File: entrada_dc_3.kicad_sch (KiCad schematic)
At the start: 4 parts

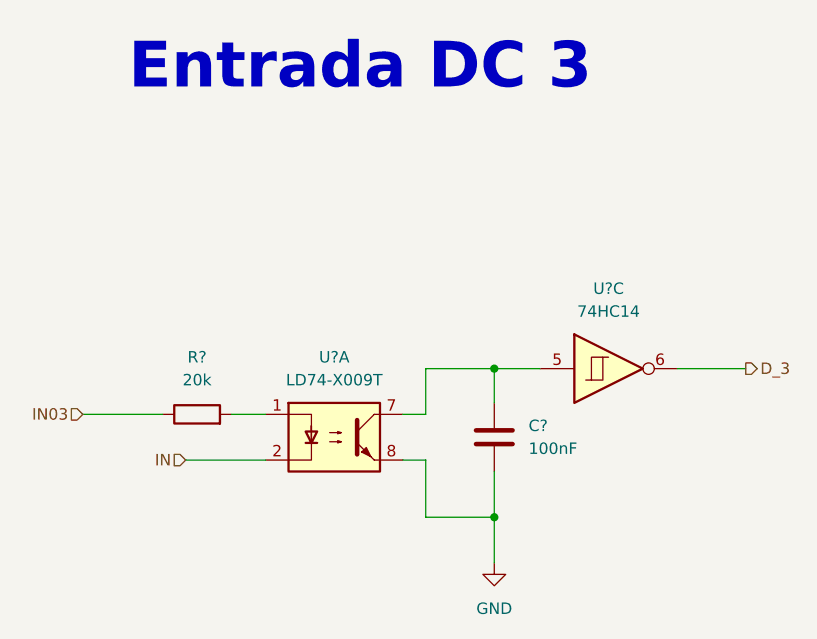
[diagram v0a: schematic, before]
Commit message: input/output separadas
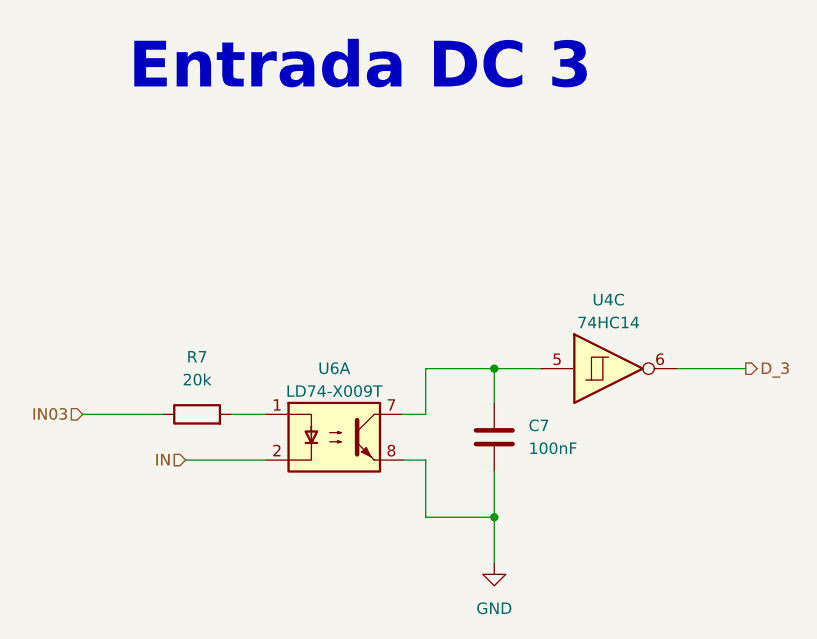
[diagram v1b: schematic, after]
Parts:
- gave numbers to parts that had none: 4
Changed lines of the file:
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@@
 (kicad_sch (version 20221004) (generator eeschema)
   (paper "A4" portrait)
+  (title_block
+    (date "2022-10-09")
+    (rev "José Luis Laica")
+  )
   (junction (at 114.3 116.84) (diameter 0) (color 0 0 0 0)
   )
@@
   (symbol (lib_id "74xx:74HC14") (at 127 116.84 0) (unit 3)
     (in_bom yes) (on_board yes) (dnp no) (fields_autoplaced)
-    (property "Reference" "U?" (at 127 107.95 0)
-      (effects (font (size 1.27 1.27)))
-    )
-    (property "Value" "74HC14" (at 127 110.49 0)
+    (property "Reference" "U4" (at 127 109.22 0)
+      (effects (font (size 1.27 1.27)))
+    )
+    (property "Value" "74HC14" (at 127 111.76 0)
       (effects (font (size 1.27 1.27)))
     )
@@
       (project "PLC 32 V2"
         (path "/d17a54f1-6eda-453f-95e1-42a53b02a1c3/37705a02-34a8-4a29-9845-d4c3245415f3"
-          (reference "U?") (unit 3) (value "74HC14") (footprint "Package_SO:SOIC-14W_7.5x9mm_P1.27mm")
+          (reference "U4") (unit 3) (value "74HC14") (footprint "Package_SO:SOIC-14W_7.5x9mm_P1.27mm")
         )
       )
@@
   (symbol (lib_id "Device:R") (at 81.28 121.92 90) (unit 1)
     (in_bom yes) (on_board yes) (dnp no) (fields_autoplaced)
-    (property "Reference" "R?" (at 81.28 115.57 90)
+    (property "Reference" "R7" (at 81.28 115.57 90)
       (effects (font (size 1.27 1.27)))
     )
@@
       (project "PLC 32 V2"
         (path "/d17a54f1-6eda-453f-95e1-42a53b02a1c3/37705a02-34a8-4a29-9845-d4c3245415f3"
-          (reference "R?") (unit 1) (value "20k") (footprint "Resistor_SMD:R_0603_1608Metric")
+          (reference "R7") (unit 1) (value "20k") (footprint "Resistor_SMD:R_0603_1608Metric")
         )
       )
@@
   (symbol (lib_id "power:GND") (at 114.3 138.43 0) (unit 1)
     (in_bom yes) (on_board yes) (dnp no) (fields_autoplaced)
-    (property "Reference" "#PWR?" (at 114.3 144.78 0)
+    (property "Reference" "#PWR08" (at 114.3 144.78 0)
       (effects (font (size 1.27 1.27)) hide)
     )
@@
       (project "PLC 32 V2"
         (path "/d17a54f1-6eda-453f-95e1-42a53b02a1c3/37705a02-34a8-4a29-9845-d4c3245415f3"
-          (reference "#PWR?") (unit 1) (value "GND") (footprint "")
+          (reference "#PWR08") (unit 1) (value "GND") (footprint "")
         )
       )
@@
   (symbol (lib_id "Isolator:ILD74") (at 96.52 124.46 0) (unit 1)
     (in_bom yes) (on_board yes) (dnp no) (fields_autoplaced)
-    (property "Reference" "U?" (at 96.52 115.57 0)
-      (effects (font (size 1.27 1.27)))
-    )
-    (property "Value" "LD74-X009T" (at 96.52 118.11 0)
+    (property "Reference" "U6" (at 96.52 116.84 0)
+      (effects (font (size 1.27 1.27)))
+    )
+    (property "Value" "LD74-X009T" (at 96.52 119.38 0)
       (effects (font (size 1.27 1.27)))
     )
@@
       (project "PLC 32 V2"
         (path "/d17a54f1-6eda-453f-95e1-42a53b02a1c3/37705a02-34a8-4a29-9845-d4c3245415f3"
-          (reference "U?") (unit 1) (value "LD74-X009T") (footprint "Package_DIP:DIP-8_W8.89mm_SMDSocket_LongPads")
+          (reference "U6") (unit 1) (value "LD74-X009T") (footprint "Package_DIP:DIP-8_W8.89mm_SMDSocket_LongPads")
         )
       )
@@
   (symbol (lib_id "Device:C") (at 114.3 124.46 0) (unit 1)
     (in_bom yes) (on_board yes) (dnp no) (fields_autoplaced)
-    (property "Reference" "C?" (at 118.11 123.1899 0)
+    (property "Reference" "C7" (at 118.11 123.1899 0)
       (effects (font (size 1.27 1.27)) (justify left))
     )
@@
       (project "PLC 32 V2"
         (path "/d17a54f1-6eda-453f-95e1-42a53b02a1c3/37705a02-34a8-4a29-9845-d4c3245415f3"
-          (reference "C?") (unit 1) (value "100nF") (footprint "Capacitor_SMD:C_0402_1005Metric")
-        )
-      )
+          (reference "C7") (unit 1) (value "100nF") (footprint "Capacitor_SMD:C_0402_1005Metric")
+        )
+      )

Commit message: add
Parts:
- renumbered C7 to C8, R7 to R37, U4 to U7, U6 to U9
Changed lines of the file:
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@@
   (symbol (lib_id "74xx:74HC14") (at 127 116.84 0) (unit 3)
     (in_bom yes) (on_board yes) (dnp no) (fields_autoplaced)
-    (property "Reference" "U4" (at 127 109.22 0)
+    (property "Reference" "U7" (at 127 109.22 0)
       (effects (font (size 1.27 1.27)))
     )
@@
       (project "PLC 32 V2"
         (path "/d17a54f1-6eda-453f-95e1-42a53b02a1c3/37705a02-34a8-4a29-9845-d4c3245415f3"
-          (reference "U4") (unit 3) (value "74HC14") (footprint "Package_SO:SOIC-14W_7.5x9mm_P1.27mm")
+          (reference "U7") (unit 3) (value "74HC14") (footprint "Package_SO:SOIC-14W_7.5x9mm_P1.27mm")
         )
       )
@@
   (symbol (lib_id "Device:R") (at 81.28 121.92 90) (unit 1)
     (in_bom yes) (on_board yes) (dnp no) (fields_autoplaced)
-    (property "Reference" "R7" (at 81.28 115.57 90)
+    (property "Reference" "R37" (at 81.28 115.57 90)
       (effects (font (size 1.27 1.27)))
     )
@@
       (project "PLC 32 V2"
         (path "/d17a54f1-6eda-453f-95e1-42a53b02a1c3/37705a02-34a8-4a29-9845-d4c3245415f3"
-          (reference "R7") (unit 1) (value "20k") (footprint "Resistor_SMD:R_0603_1608Metric")
+          (reference "R37") (unit 1) (value "20k") (footprint "Resistor_SMD:R_0603_1608Metric")
         )
       )
@@
   (symbol (lib_id "Isolator:ILD74") (at 96.52 124.46 0) (unit 1)
     (in_bom yes) (on_board yes) (dnp no) (fields_autoplaced)
-    (property "Reference" "U6" (at 96.52 116.84 0)
+    (property "Reference" "U9" (at 96.52 116.84 0)
       (effects (font (size 1.27 1.27)))
     )
@@
       (project "PLC 32 V2"
         (path "/d17a54f1-6eda-453f-95e1-42a53b02a1c3/37705a02-34a8-4a29-9845-d4c3245415f3"
-          (reference "U6") (unit 1) (value "LD74-X009T") (footprint "Package_DIP:DIP-8_W8.89mm_SMDSocket_LongPads")
+          (reference "U9") (unit 1) (value "LD74-X009T") (footprint "Package_DIP:DIP-8_W8.89mm_SMDSocket_LongPads")
         )
       )
@@
   (symbol (lib_id "Device:C") (at 114.3 124.46 0) (unit 1)
     (in_bom yes) (on_board yes) (dnp no) (fields_autoplaced)
-    (property "Reference" "C7" (at 118.11 123.1899 0)
+    (property "Reference" "C8" (at 118.11 123.1899 0)
       (effects (font (size 1.27 1.27)) (justify left))
     )
@@
       (project "PLC 32 V2"
         (path "/d17a54f1-6eda-453f-95e1-42a53b02a1c3/37705a02-34a8-4a29-9845-d4c3245415f3"
-          (reference "C7") (unit 1) (value "100nF") (footprint "Capacitor_SMD:C_0402_1005Metric")
+          (reference "C8") (unit 1) (value "100nF") (footprint "Capacitor_SMD:C_0402_1005Metric")
         )
       )
